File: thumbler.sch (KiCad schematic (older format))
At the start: 182 parts, among them J5 USB_B_Micro, J6 Conn_01x04, SW1 SW_Push, SW2 SW_DIP_x01, U1 MCP1700-3302E_SOT89, U2 STM32F072C8Tx

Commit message: add current limiting resistors to USB D+/-
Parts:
- removed C? (x3): 1u, Capacitor_SMD:C_0805_2012Metric_Pad1.18x1.45mm_HandSolder, symbol Device:C_Small
- removed C? (x2): 4u7, Capacitor_SMD:C_0805_2012Metric_Pad1.18x1.45mm_HandSolder, symbol Device:C_Small
- removed C? (x3): 100n, Capacitor_SMD:C_0805_2012Metric_Pad1.18x1.45mm_HandSolder, symbol Device:C_Small
- removed C?: 10n, Capacitor_SMD:C_0805_2012Metric_Pad1.18x1.45mm_HandSolder, symbol Device:C_Small
- removed D?: RED, LED_SMD:LED_1206_3216Metric_Pad1.42x1.75mm_HandSolder, symbol Device:LED_Small
- removed FB?: 90R @ 100MHz, Inductor_SMD:L_0805_2012Metric_Pad1.15x1.40mm_HandSolder, symbol Device:Ferrite_Bead_Small
- removed J?: USB_B_Micro, symbol Connector:USB_B_Micro
- removed R?: 1K, Resistor_SMD:R_0805_2012Metric_Pad1.20x1.40mm_HandSolder, symbol Device:R_Small_US
- removed U?: MCP1700-3302E_SOT89, Package_TO_SOT_SMD:SOT-89-3, symbol Regulator_Linear:MCP1700-3302E_SOT89
- added C? (x2): 4u7, Capacitor_SMD:C_0805_2012Metric_Pad1.18x1.45mm_HandSolder, symbol Device:C_Small
- added C? (x3): 100n, Capacitor_SMD:C_0805_2012Metric_Pad1.18x1.45mm_HandSolder, symbol Device:C_Small
- added C? (x3): 1u, Capacitor_SMD:C_0805_2012Metric_Pad1.18x1.45mm_HandSolder, symbol Device:C_Small
- added C?: 10n, Capacitor_SMD:C_0805_2012Metric_Pad1.18x1.45mm_HandSolder, symbol Device:C_Small
- added D?: RED, LED_SMD:LED_1206_3216Metric_Pad1.42x1.75mm_HandSolder, symbol Device:LED_Small
- added FB?: 90R @ 100MHz, Inductor_SMD:L_0805_2012Metric_Pad1.15x1.40mm_HandSolder, symbol Device:Ferrite_Bead_Small
- added J?: USB_B_Micro, symbol Connector:USB_B_Micro
- added R? (x4): 20R, symbol Device:R_Small_US
- added R?: 1K, Resistor_SMD:R_0805_2012Metric_Pad1.20x1.40mm_HandSolder, symbol Device:R_Small_US
- added U?: MCP1700-3302E_SOT89, Package_TO_SOT_SMD:SOT-89-3, symbol Regulator_Linear:MCP1700-3302E_SOT89
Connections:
- wire segments 443 -> 451
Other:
- moved on the sheet: C2, C3, C4, C5, C6, C7, C?, D63, FB1, R4, U1

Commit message: thumb v0, options, optimizations
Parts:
- removed C?: C_Small, symbol Device:C_Small
- removed J?: AudioJack4, Connector_Audio:Jack_6.35mm_Neutrik_NMJ6HCD2_Horizontal, symbol Connector:AudioJack4
- removed R1: 10K, Resistor_SMD:R_0805_2012Metric_Pad1.20x1.40mm_HandSolder, symbol Device:R_Small_US
- removed SW2: SW_DIP_x01, symbol Switch:SW_DIP_x01
- added C12: C_Small, symbol Device:C_Small
- added J?: AudioJack4, Connector_Audio:Jack_6.35mm_Neutrik_NMJ6HCD2_Horizontal, symbol Connector:AudioJack4
- added J?: Conn_01x04, symbol Connector_Generic:Conn_01x04
- added R?: 10K, symbol Device:R_Small_US
- added R? (x17): 470R, symbol Device:R_Small_US
- added SW?: SW_DIP_x05, symbol Switch:SW_DIP_x05
- added TP? (x4): TestPoint, symbol Connector:TestPoint
- gave numbers to parts that had none: 29
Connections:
- net labels added: L_COL8, L_HAND_SET, L_OPT1, L_OPT2, L_OPT3, L_OPT4, L_PTR_Z, L_RX, L_TX, R_RX, R_TX
- net labels removed: +3.3VA, RX, TX
- wire segments 451 -> 504
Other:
- note added: "Current limiting resistors \nprotect against software \nerrors that might connect\ntwo outputs (e.g. if a row \nand column pin got mixed \nup). After testing, they can \nbe replaced with 0Rs."
- note added: "NB: Avoid (un)plugging when powered on.\nResistor helps protect 5V-GND shorts.\nTODO: Smoothing cap for transients?"
- note added: "NB: RX/TX must be flipped between left \nand right side for USART connection.\n"
- note added: "Need to select capacitor size given STM32 \nADC input impedence requirement of 50K"
- note added: "Option Select"
- note added: "USART"
- note added: "https://www.ti.com/lit/an/spna061/spna061.pdf"
- note removed: "Boot Select"
- note removed: "Leader/Follower Select\n(Disconnects USB data, need leader mode to flash w/ DFU)"
- note removed: "NB: 5V must be sleeve to avoid unwanted\nvoltage when (un)plugging"
- moved on the sheet: C11, C9, D64, D65, D66, J1, J6, R2, S63, S64, S65, S66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

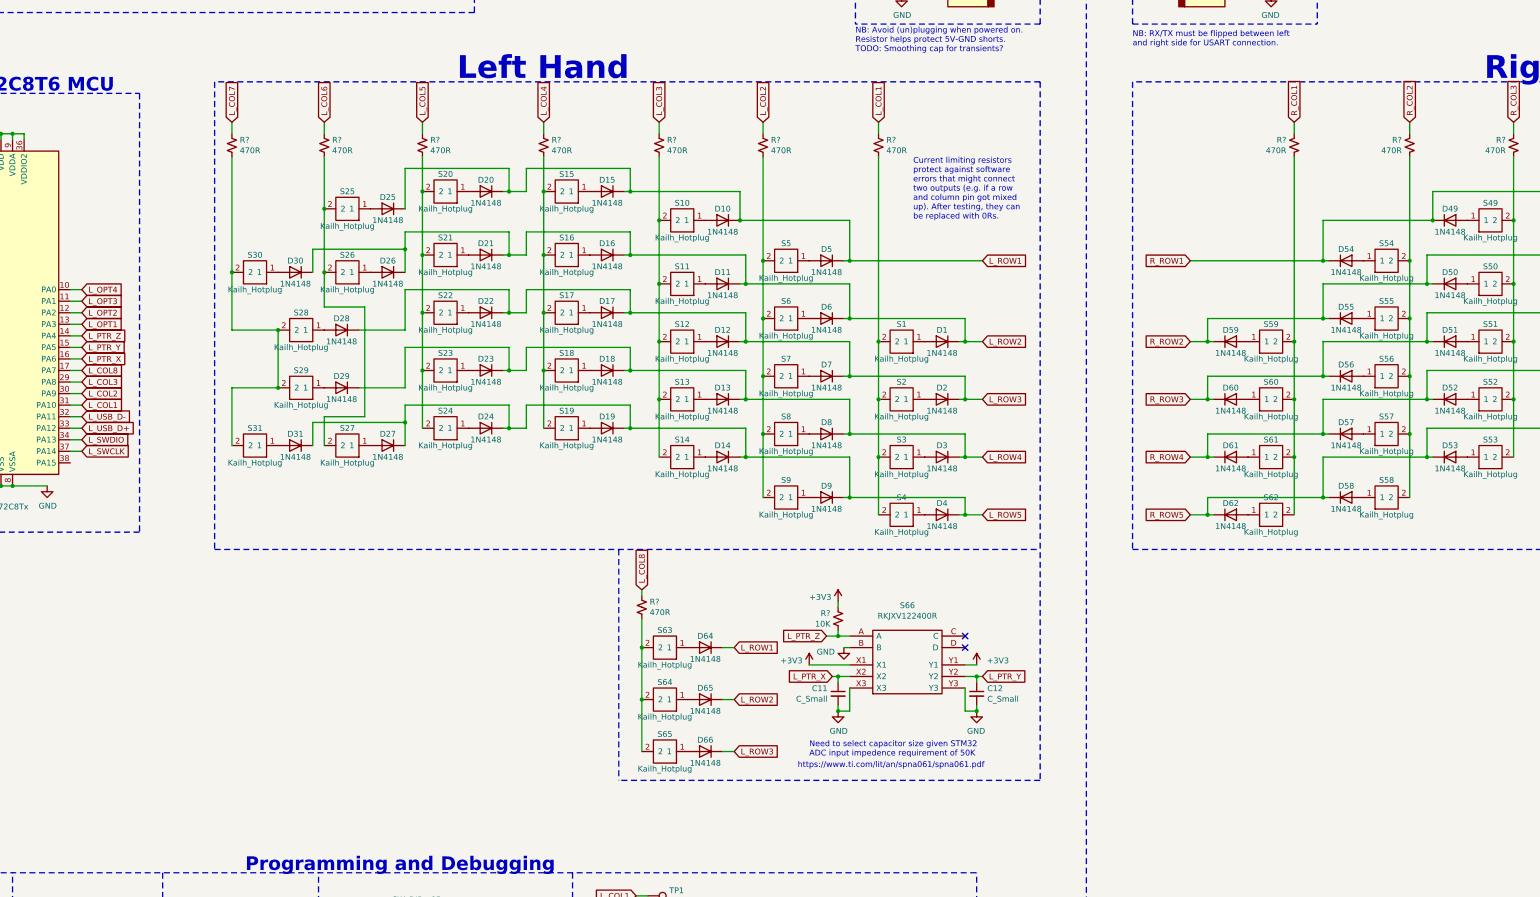
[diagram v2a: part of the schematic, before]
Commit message: add footprint for ANO
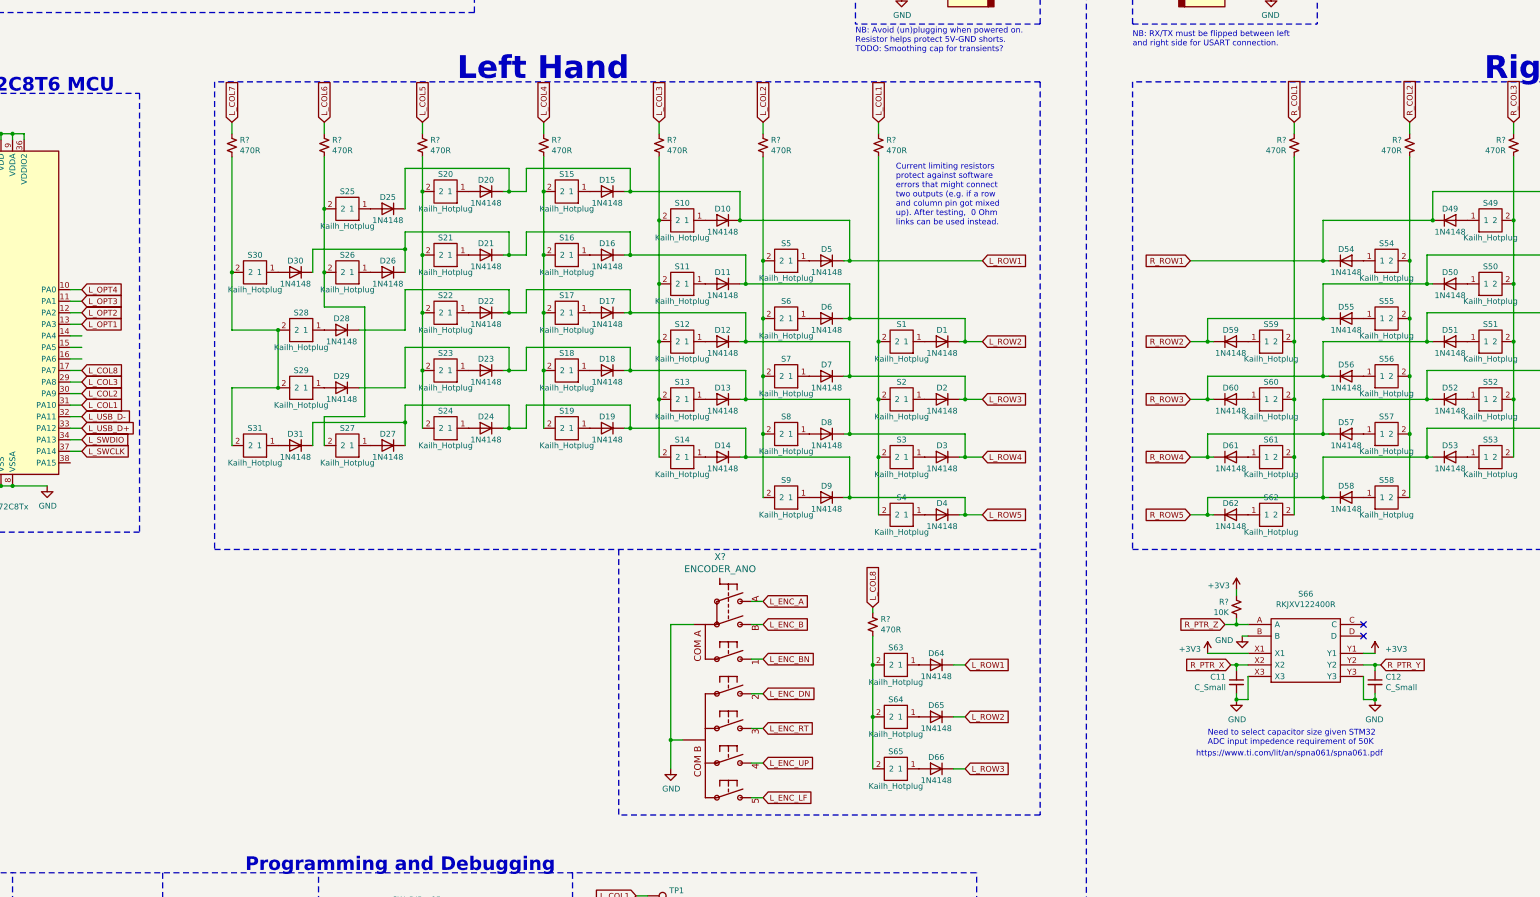
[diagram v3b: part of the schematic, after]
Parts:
- added X?: ENCODER_ANO, symbol thumbler-eagle-import:ENCODER_ANO
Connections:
- net GND: now also X?.COM_A (COMA), X?.COM_B
- net L_PTR_X: no longer C11.1, S66.X2, U2.16 (PA6)
- net L_PTR_Y: no longer C12.1, S66.Y2, U2.15 (PA5)
- net L_PTR_Z: no longer R?.1, S66.A, U2.14 (PA4)
- new net L_ENC_A: X?.A
- new net L_ENC_B: X?.B
- new net L_ENC_BN: X?.S1 (1)
- new net L_ENC_DN: X?.S2
- new net L_ENC_LF: X?.S5
- new net L_ENC_RT: X?.S3
- new net L_ENC_UP: X?.S4
- new net R_PTR_X: C11.1, S66.X2
- new net R_PTR_Y: C12.1, S66.Y2
- new net R_PTR_Z: R?.1, S66.A
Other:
- note added: "Current limiting resistors \nprotect against software \nerrors that might connect\ntwo outputs (e.g. if a row \nand column pin got mixed \nup). After testing, 0 Ohm \nlinks can be used instead."
- note removed: "Current limiting resistors \nprotect against software \nerrors that might connect\ntwo outputs (e.g. if a row \nand column pin got mixed \nup). After testing, they can \nbe replaced with 0Rs."
- moved on the sheet: C11, C12, D64, D65, D66, R?, S63, S64, S65, S66

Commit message: v0?
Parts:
- removed J1, J?: AudioJack4, Connector_Audio:Jack_6.35mm_Neutrik_NMJ6HCD2_Horizontal, symbol Connector:AudioJack4
- removed R? (x2): 470R, symbol Device:R_Small_US
- added C?: 100n, Capacitor_SMD:C_0805_2012Metric_Pad1.18x1.45mm_HandSolder, symbol Device:C_Small
- added D? (x3): 1N4148, Diode_THT:D_DO-35_SOD27_P7.62mm_Horizontal, symbol Diode:1N4148
- added D? (x3): WHITE, LED_SMD:LED_1206_3216Metric_Pad1.42x1.75mm_HandSolder, symbol Device:LED_Small
- added J? (x2): DIN-5_180degree, symbol Connector:DIN-5_180degree
- added J? (x2): Conn_01x04, symbol Connector_Generic:Conn_01x04
- added R?: 470R, symbol Device:R_Small_US
- added R?: 10K, Resistor_SMD:R_0805_2012Metric_Pad1.20x1.40mm_HandSolder, symbol Device:R_Small_US
- added R? (x3): 1K, Resistor_SMD:R_0805_2012Metric_Pad1.20x1.40mm_HandSolder, symbol Device:R_Small_US
- added S? (x3): Kailh_Hotplug, keyswitches:Kailh_socket_MX_platemount, symbol kailh_hotplug_mx_plate:Kailh_Hotplug
- added SW?: SW_DIP_x05, symbol Switch:SW_DIP_x05
- added SW?: SW_Push, symbol Switch:SW_Push
- added TP? (x20): TestPoint, symbol Connector:TestPoint
- added U?: STM32F072C8Tx, Package_QFP:LQFP-48_7x7mm_P0.5mm, symbol MCU_ST_STM32F0:STM32F072C8Tx
- C11, C12: value C_Small -> Cext
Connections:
- net L_PTR_X is gone; now on net L_ENC_BN: TP?.1
- net L_PTR_Y is gone; now on net L_ENC_DN: TP?.1
- net L_PTR_Z is gone; now on net L_ENC_RT: TP?.1
- net +3V3: now also D?.2 (A), D?.2 (A), D?.2 (A), J?.1 (Pin_1), J?.1 (Pin_1), SW?.5, U?.1 (VBAT), U?.24 (VDD), U?.36 (VDDIO2), U?.48 (VDD), U?.9 (VDDA)
- net +5V: now also J?.4, J?.4
- net GND: now also C?.2, J?.1, J?.1, J?.4 (Pin_4), J?.4 (Pin_4), R?.2, SW?.1, SW?.1, SW?.2, SW?.3, SW?.4, U?.23 (VSS), U?.35 (VSS), U?.46 (PB9), U?.47 (VSS), U?.8 (VSSA)
- net L_COL8: now also U2.15 (PA5); no longer U2.17 (PA7)
- net L_ENC_A: now also U2.16 (PA6), TP?.1
- net L_ENC_B: now also U2.17 (PA7), TP?.1
- net L_ENC_BN: now also U2.38 (PA15)
- net L_ENC_DN: now also U2.39 (PB3)
- net L_ENC_LF: now also U2.45 (PB8), TP?.1
- net L_ENC_RT: now also U2.40 (PB4)
- net L_ENC_UP: now also U2.41 (PB5), TP?.1
- net L_RX: now also J?.3
- net L_TX: now also J?.5
- net R_COL1: now also TP?.1, U?.31 (PA10)
- net R_COL2: now also TP?.1, U?.30 (PA9)
- net R_COL3: now also TP?.1, U?.29 (PA8)
- net R_COL4: now also TP?.1, U?.28 (PB15)
- net R_COL5: now also TP?.1, U?.27 (PB14)
- net R_COL6: now also TP?.1, U?.26 (PB13)
- net R_COL7: now also TP?.1, U?.25 (PB12)
- net R_PTR_X: now also TP?.1, U?.16 (PA6)
- net R_PTR_Y: now also TP?.1, U?.17 (PA7)
- net R_PTR_Z: now also TP?.1, U?.38 (PA15)
- net R_ROW1: now also D?.1 (K), TP?.1, U?.18 (PB0)
- net R_ROW2: now also D?.1 (K), TP?.1, U?.19 (PB1)
- net R_ROW3: now also D?.1 (K), TP?.1, U?.20 (PB2)
- net R_ROW4: now also TP?.1, U?.21 (PB10)
- net R_ROW5: now also TP?.1, U?.22 (PB11)
- net R_RX: now also J?.2 (Pin_2), J?.5, U?.43 (PB7)
- net R_TX: now also J?.3, J?.3 (Pin_3), U?.42 (PB6)
- net R_USB_D+: now also U?.33 (PA12)
- net R_USB_D-: now also U?.32 (PA11)
- net L_NRST renamed ~RST
- net ~RST: now also C?.1, J?.2, J?.2, SW?.2, U?.7 (NRST)
- new net: D?.2 (A), S?.1 (x3)
- new net: R?.2, S?.2, S?.2, S?.2
- new net: D?.1 (K), R?.1 (x3)
- new net R_BOOT0: R?.1, SW?.6, U?.44 (BOOT0)
- new net R_COL8: R?.1, TP?.1, U?.15 (PA5)
- new net R_LED1: R?.2, U?.39 (PB3)
- new net R_LED2: R?.2, U?.40 (PB4)
- new net R_LED3: R?.2, U?.41 (PB5)
- new net R_OPT1: SW?.7, U?.13 (PA3)
- new net R_OPT2: SW?.8, U?.12 (PA2)
- new net R_OPT3: SW?.9, U?.11 (PA1)
- new net R_OPT4: SW?.10, U?.10 (PA0)
- new net R_SWCLK: J?.3 (Pin_3), U?.37 (PA14)
- new net R_SWDIO: J?.2 (Pin_2), U?.34 (PA13)
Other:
- note added: "Current limiting resistors \nprotect against software \nerrors (for instance, if you\naccidentally made a row\npin into a column, it could \nbe set to low output and \nthen scanned by a column \npin pulling high). If you are \nbrave, 0R links can be used \ninstead. 470R limits to 7mA, \nwithin STM32 rated GPIO \ncapacity."
- note added: "DIN5 Link"
- note added: "Input Test Points"
- note added: "NB: Right side USB for DFU firmware updates only! Generally DIN5 link will provide +5V."
- note added: "Need to select Cext for STM32 ADC (8pF Csamp)\nhttps://www.ti.com/lit/an/spna061/spna061.pdf"
- note added: "Status LEDs"
- note removed: "Current limiting resistors \nprotect against software \nerrors that might connect\ntwo outputs (e.g. if a row \nand column pin got mixed \nup). After testing, 0 Ohm \nlinks can be used instead."
- note removed: "Key Test Points"
- note removed: "NB: Avoid (un)plugging when powered on.\nResistor helps protect 5V-GND shorts.\nTODO: Smoothing cap for transients?"
- note removed: "Need to select capacitor size given STM32 \nADC input impedence requirement of 50K"
- note removed: "TRRS Link"
- note removed: "https://www.ti.com/lit/an/spna061/spna061.pdf"
- moved on the sheet: C1, C10, C11, C12, C13, C14, C15, C16, C17, C18, C19, C2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

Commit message: more protection, more footprints
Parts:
- added D74, D75: B5819W, Diode_SMD:D_SOD-123, symbol Device:D_Schottky
- added F1, F2: 350mA, Resistor_SMD:R_1812_4532Metric_Pad1.30x3.40mm_HandSolder, symbol Device:Polyfuse_Small
- added JP1: SolderJumper_2_Open, Jumper:SolderJumper-2_P1.3mm_Open_TrianglePad1.0x1.5mm, symbol Jumper:SolderJumper_2_Open
- C11, C12: footprint (none) -> Capacitor_SMD:C_0805_2012Metric_Pad1.18x1.45mm_HandSolder
- J1, J4, J8: renamed from J?; footprint (none) -> Connector_PinHeader_2.54mm:PinHeader_2x02_P2.54mm_Vertical
- J2, J7: renamed from J?; footprint (none) -> Connector_DIN:DIN5_180_CP-2350
- J6: footprint (none) -> Connector_PinHeader_2.54mm:PinHeader_2x02_P2.54mm_Vertical
- R1, R10, R11, R12, R13, R14, R15, R16, R17, R18, R19, R22, R24, R26, R27, R28, R9: renamed from R?; footprint (none) -> Resistor_SMD:R_0805_2012Metric_Pad1.20x1.40mm_HandSolder
- R3, R5, R6, R7: value 20R -> 22R; footprint (none) -> Resistor_SMD:R_0805_2012Metric_Pad1.20x1.40mm_HandSolder
- SW1: footprint (none) -> Button_Switch_THT:SW_PUSH-12mm
- SW2, SW4: renamed from SW?; footprint (none) -> Button_Switch_THT:SW_DIP_SPSTx05_Slide_9.78x14.88mm_W7.62mm_P2.54mm
- SW3: renamed from SW?; footprint (none) -> Button_Switch_THT:SW_PUSH-12mm
- TP1, TP10, TP11, TP12, TP2, TP3, TP4, TP5, TP6, TP7, TP8, TP9: footprint (none) -> TestPoint:TestPoint_Pad_D2.0mm
- TP13, TP14, TP15, TP16, TP17, TP18, TP19, TP20, TP21, TP22, TP23, TP24, TP25, TP26, TP27, TP28, TP29, TP30, TP31, TP32, TP33, TP34, TP35, TP36: renamed from TP?; footprint (none) -> TestPoint:TestPoint_Pad_D2.0mm
- X1: renamed from X?; footprint (none) -> Rotary_Encoder:ENCODER_ANO
- gave numbers to parts that had none: 15
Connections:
- net +5V: now also F1.1, F2.2; no longer FB1.2, FB2.2
- net ~RST: now also JP1.2 (B); no longer J2.2
- new net: D75.1 (K), FB2.2
- new net: J2.2, JP1.1 (A)
- new net: D74.1 (K), FB1.2
- new net: D75.2 (A), F2.1
- new net: D74.2 (A), F1.2
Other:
- note added: "Not sure if tying reset together is a good \nidea or not. Solder jumper in case it's a \nbad idea."
- moved on the sheet: C1, C10, C2, C3, C4, C5, C6, C7, C8, D63, D68, D72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

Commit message: footprints done
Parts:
- removed R16: 10K, Resistor_SMD:R_0805_2012Metric_Pad1.20x1.40mm_HandSolder, symbol Device:R_Small_US
- added TP37, TP38: TestPoint, TestPoint:TestPoint_Pad_D2.0mm, symbol Connector:TestPoint
- J3, J5: footprint (none) -> Connector_USB:USB_Micro-B_HRO_U-F-M5SS-W-1
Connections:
- net +5V: now also D74.1 (K), D75.1 (K), FB1.2, FB2.2, TP37.1, TP38.1; no longer F1.1, F2.2, J3.1 (VBUS), J5.1 (VBUS)
- net at F2.1: now also J3.1 (VBUS); no longer D75.2 (A)
- new net: F1.1, J5.1 (VBUS)
- new net: D75.2 (A), F2.2
- no-connect marks 6 -> 19
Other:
- note added: "Current limiting resistors \nprotect against software \nerrors (for instance, if you\naccidentally made a row\npin into a column, it could \nbe set to high output and \nthen scanned by a column \npin pulling low). If you are \nbrave, 0R links can be used \ninstead. 470R limits to 7mA, \nwithin STM32 rated GPIO \ncapacity."
- note added: "Not sure if tying reset together is needed.\nSolder jumper in case it's a bad idea."
- note removed: "Current limiting resistors \nprotect against software \nerrors (for instance, if you\naccidentally made a row\npin into a column, it could \nbe set to low output and \nthen scanned by a column \npin pulling high). If you are \nbrave, 0R links can be used \ninstead. 470R limits to 7mA, \nwithin STM32 rated GPIO \ncapacity."
- note removed: "Not sure if tying reset together is a good \nidea or not. Solder jumper in case it's a \nbad idea."
- moved on the sheet: D74, F1, R3, R5
